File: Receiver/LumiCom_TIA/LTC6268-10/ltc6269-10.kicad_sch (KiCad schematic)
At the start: 28 parts, among them J10 OUT, J7 IN, J8 Vout, J9 TEST, U2 LTC6268-10-SOT23

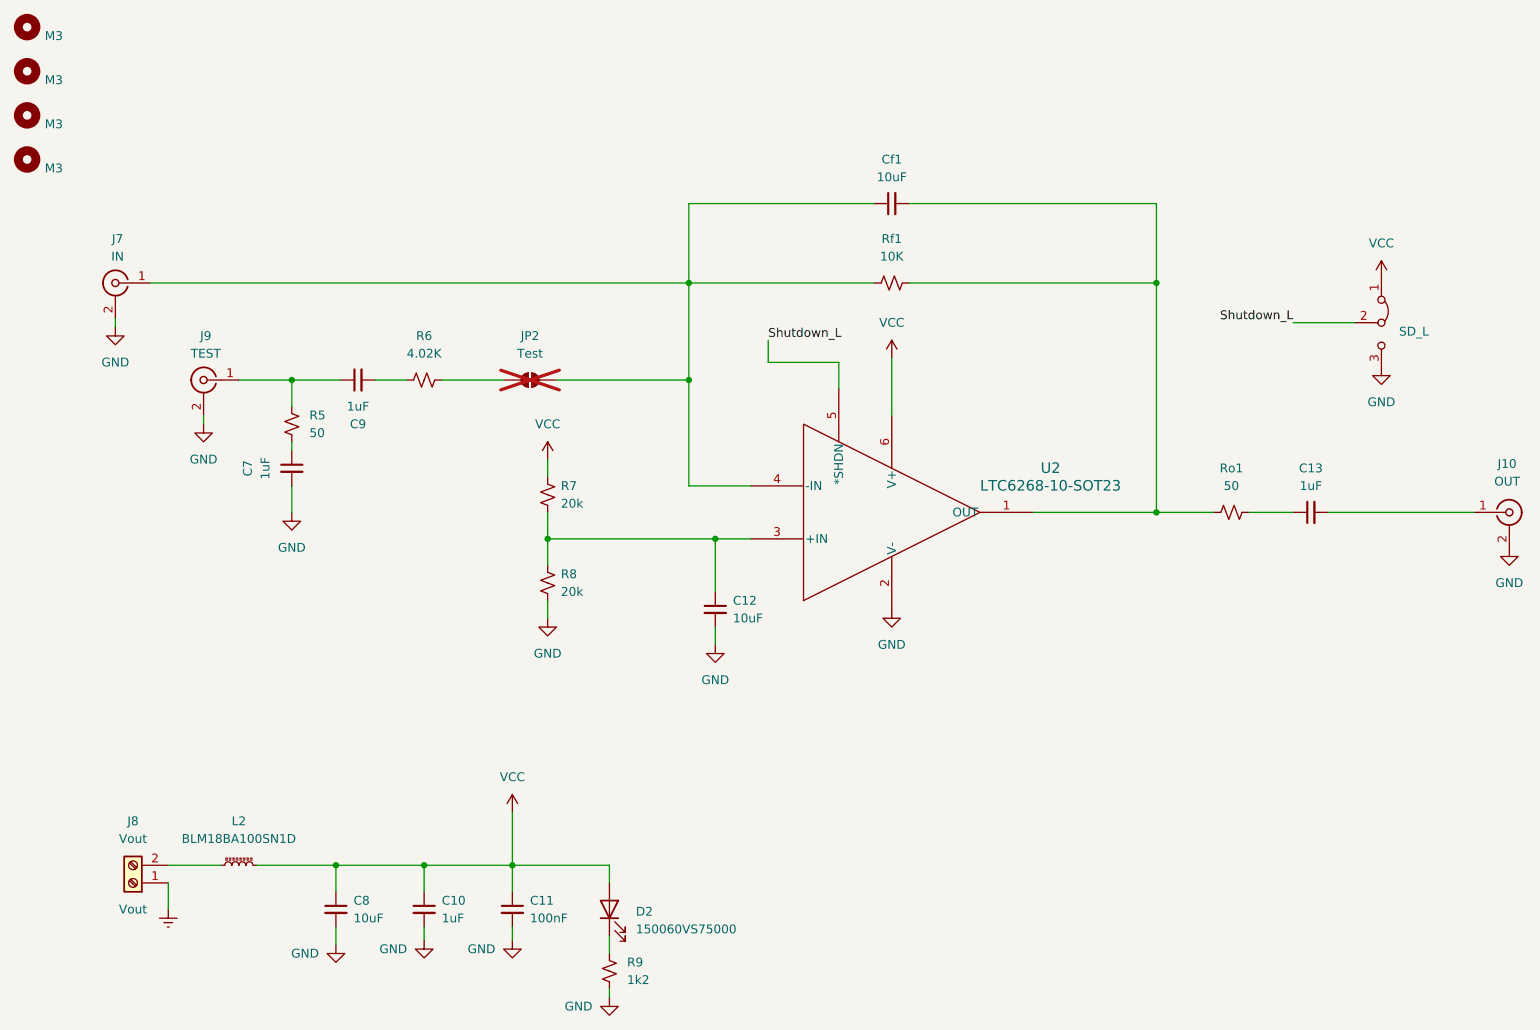
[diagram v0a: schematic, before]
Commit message: Multiple updates
SMA, Screw terminals, track widths, added some optional 0 ohm bypass resistors
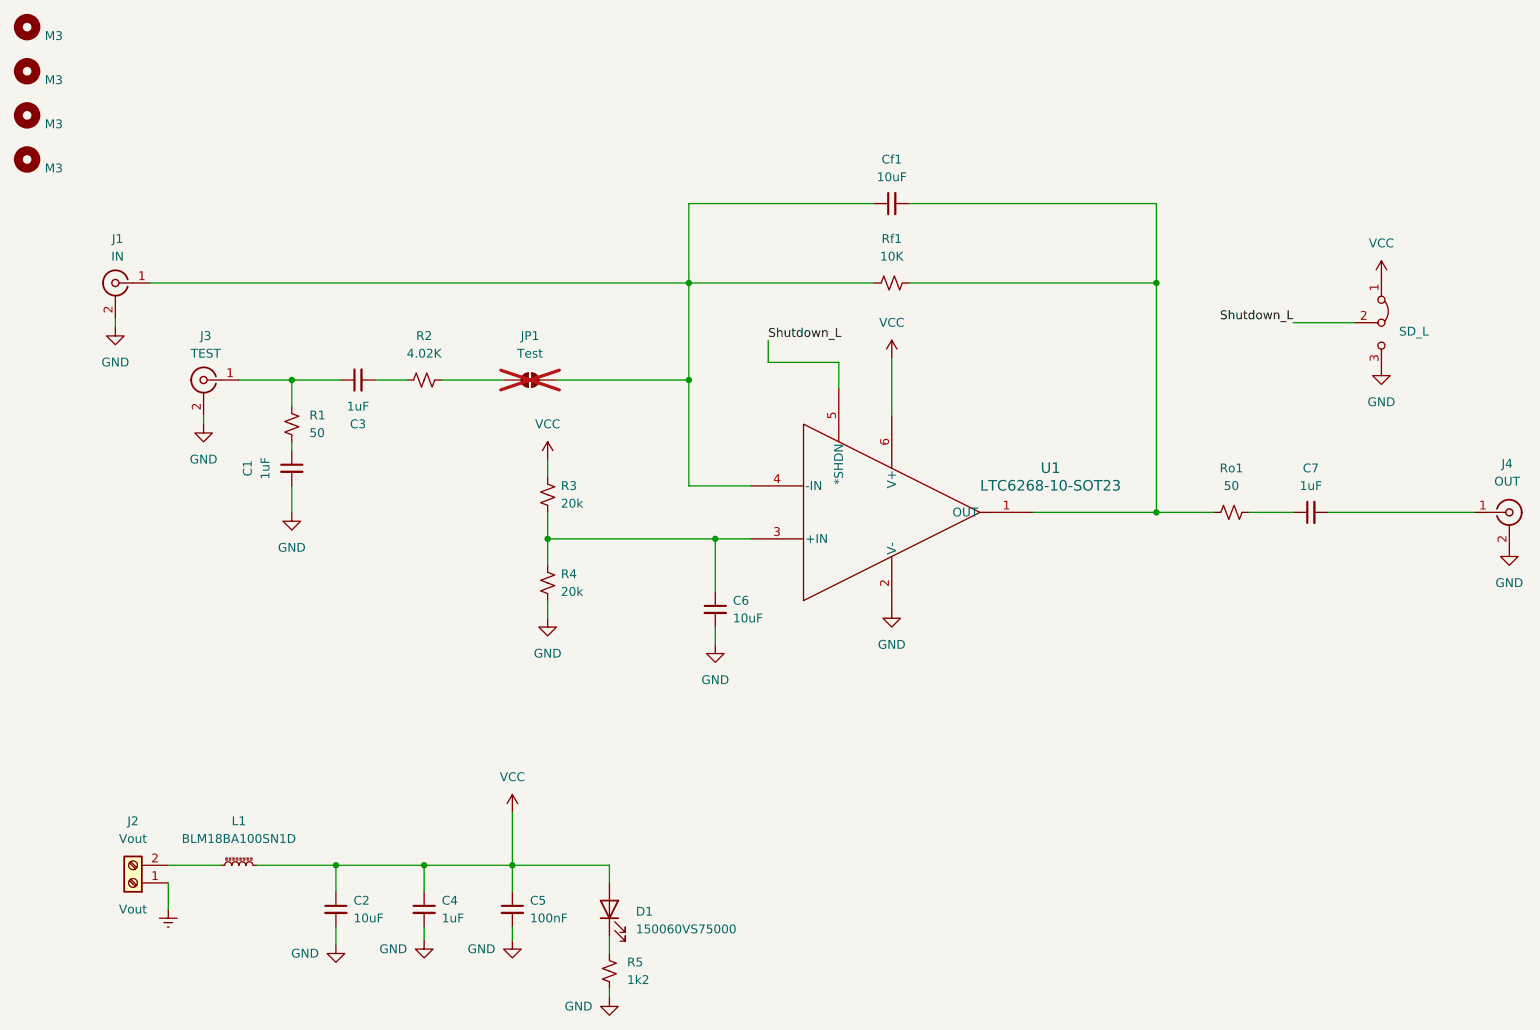
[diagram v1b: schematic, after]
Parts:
- J1: renamed from J7; footprint LumiCom_TIA:RFSOLUTIONS_CON-SMA-EDGE-S -> Connector_Coaxial:SMA_Samtec_SMA-J-P-X-ST-EM1_EdgeMount
- J3: renamed from J9; footprint LumiCom_TIA:RFSOLUTIONS_CON-SMA-EDGE-S -> Connector_Coaxial:SMA_Samtec_SMA-J-P-X-ST-EM1_EdgeMount
- J4: renamed from J10; footprint LumiCom_TIA:RFSOLUTIONS_CON-SMA-EDGE-S -> Connector_Coaxial:SMA_Samtec_SMA-J-P-X-ST-EM1_EdgeMount
- renumbered C7 to C1, C8 to C2, C9 to C3, C10 to C4, C11 to C5, C12 to C6, C13 to C7, D2 to D1, H5 to H1, H6 to H2, H7 to H3, H8 to H4, J8 to J2, JP2 to JP1, L2 to L1, R5 to R1, R6 to R2, R7 to R3, R8 to R4, R9 to R5, U2 to U1
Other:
- title: (none) -> TIA LTC6268-10
